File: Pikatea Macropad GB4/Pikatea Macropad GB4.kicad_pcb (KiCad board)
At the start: 2 copper layers, 125.1 x 25.2 mm, 28 parts, among them J1 AVR-ISP-6, J2 USB_B_Mini, J4 Conn_01x03_Male, J5 Conn_01x03_Male, J6 Conn_01x06_Male, SW1 SW_DPST, SW2 Rotary_Encoder_Switch, U1 ATMEGA32U4-EP, X1 16MHz

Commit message: update GB4
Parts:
- removed J5: Conn_01x03_Male, Connector_PinHeader_2.54mm:PinHeader_1x03_P2.54mm_Vertical
- added D2: APA-106-F5, Pikatea:TONYU-DY-S352818-RGBC, B.Cu at (149.9, 109.7)
- added D3: APA-106-F5, Pikatea:TONYU-DY-S352818-RGBC, B.Cu at (168.9, 109.7)
- added D4: APA-106-F5, Pikatea:TONYU-DY-S352818-RGBC, B.Cu at (188.0, 109.7)
- added D5: APA-106-F5, Pikatea:TONYU-DY-S352818-RGBC, B.Cu at (207.1, 109.7)
- added D6: APA-106-F5, Pikatea:TONYU-DY-S352818-RGBC, F.Cu at (220.7, 110.0)
- added D7: APA-106-F5, Pikatea:TONYU-DY-S352818-RGBC, F.Cu at (230.6, 110.3)
- D1: moved to B.Cu
- U1: footprint Package_QFP:LQFP-44_10x10mm_P0.8mm -> Package_DFN_QFN:QFN-44-1EP_7x7mm_P0.5mm_EP5.15x5.15mm_ThermalVias
- moved D1 21.3 mm to (130.8, 109.7)
- moved C3 5.36 mm to (110.9, 99.7)
- moved C6 3.73 mm to (130.9, 96.3)
- moved C4 1.35 mm to (125.6, 99.8), turned to 90 degrees
- moved R5 0.88 mm to (129.9, 93.8)
- moved C10 0.63 mm to (124.8, 102.0)
- turned MX1 to 180 degrees
- turned MX2 to 180 degrees
- turned MX3 to 180 degrees
- turned MX4 to 180 degrees
- turned MX5 to 180 degrees
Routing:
- net VBUS: track 0.00 -> 103.3 mm, vias 0 -> 7
- net /A0: track 0.00 -> 86.9 mm
- net GND: track 0.00 -> 41.5 mm, vias 0 -> 3
- net Net-(D1-Pad1): track 0.00 -> 14.6 mm
- net Net-(D4-Pad1): track 0.00 -> 14.6 mm
- net Net-(D2-Pad1): track 0.00 -> 14.6 mm
- net /D3: track 0.00 -> 13.3 mm
- net Net-(C8-Pad1): track 0.00 -> 12.6 mm
- net Net-(C7-Pad1): track 0.00 -> 11.3 mm
- net Net-(R5-Pad2): track 0.00 -> 9.35 mm
- net Net-(R4-Pad2): track 0.00 -> 9.26 mm
- net Net-(C9-Pad1): track 0.00 -> 8.24 mm
- net /D4: track 0.00 -> 7.75 mm
- net /D+: track 0.00 -> 6.50 mm
- net /D-: track 0.00 -> 5.83 mm
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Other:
- outline, holes or cut-outs redrawn

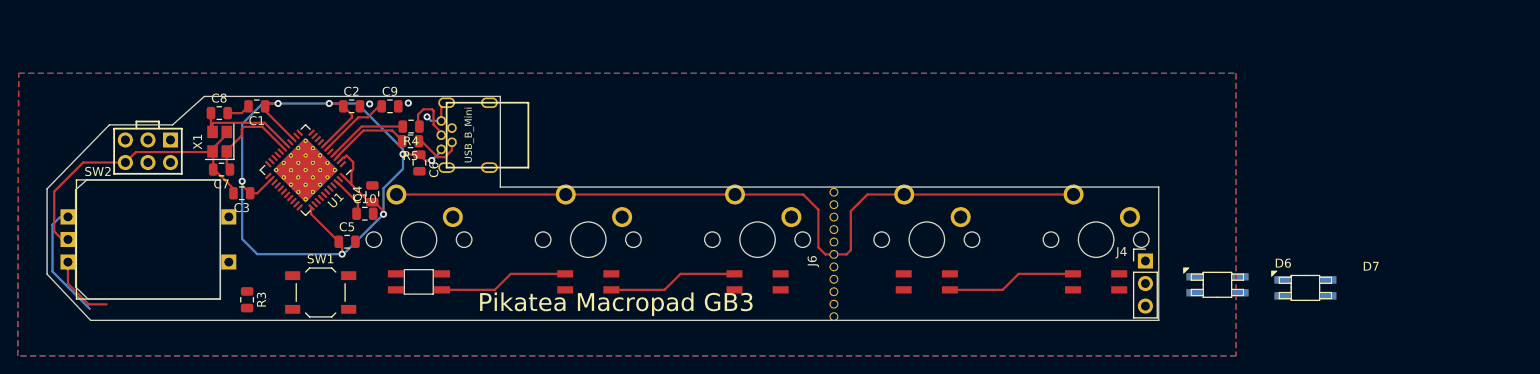
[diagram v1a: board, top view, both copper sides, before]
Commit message: update r26 and gb4
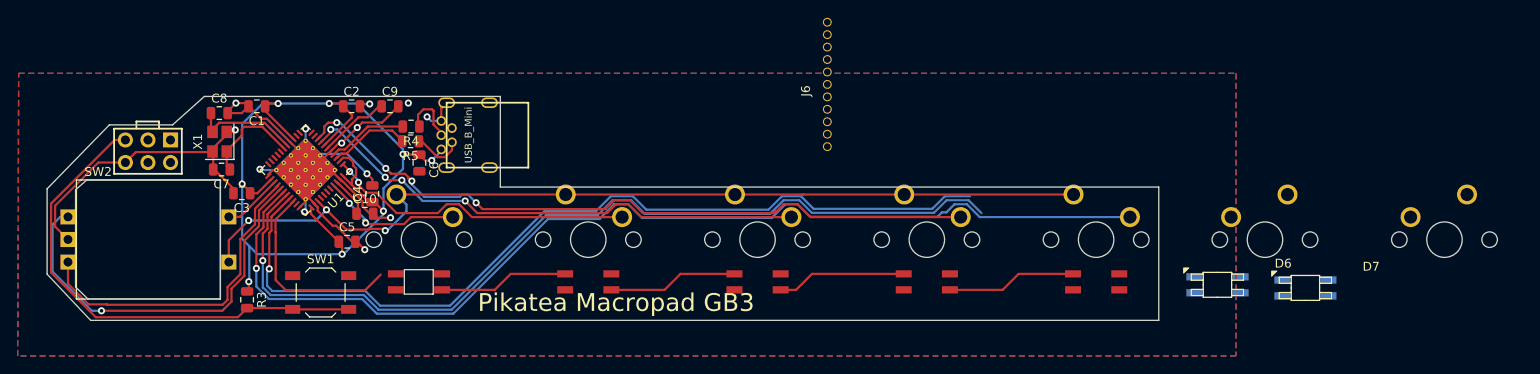
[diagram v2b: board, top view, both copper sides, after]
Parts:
- removed J4: Conn_01x03_Male, Connector_PinHeader_2.54mm:PinHeader_1x03_P2.54mm_Vertical
- added MX6: MX-LED, MX_Only:MXOnly-1U-NoLED, F.Cu at (226.1, 104.9)
- added MX7: MX-LED, MX_Only:MXOnly-1U-NoLED, F.Cu at (246.2, 104.9)
- moved J6 19.1 mm to (176.8, 87.5)
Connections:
- D1 pad 4: Net-(D1-Pad4) -> /31
- J1 pad 3: /SCK -> /D8
- J6 pad 1: GND -> Net-(J6-Pad1)
- J6 pad 2: /D8 -> Net-(J6-Pad2)
- J6 pad 3: /D6 -> Net-(J6-Pad3)
- J6 pad 4: /A0 -> Net-(J6-Pad4)
- J6 pad 5: /D1 -> Net-(J6-Pad5)
- J6 pad 6: /D0 -> Net-(J6-Pad6)
- MX5 pad 1: /D6 -> /28
- SW2 pad A: /D4 -> /D12
- SW2 pad B: /D3 -> /D6
- SW2 pad S1: /D2 -> /D4
- U1 pad 1: /D7 -> /D9
- U1 pad 28: /D8 -> /28
- U1 pad 29: /D9 -> /29
- U1 pad 31: /D5 -> /31
- U1 pad 41: /D0 -> /D5
- U1 pad 8: Net-(U1-Pad8) -> /D7
- U1 pad 9: /SCK -> /D8
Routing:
- net /28: track 0.00 -> 119.7 mm, vias 0 -> 1
- net /29: track 0.00 -> 101.6 mm, vias 0 -> 1
- net /CS: track 0.00 -> 98.6 mm, vias 0 -> 1
- net GND: track 41.5 -> 128.1 mm, vias 3 -> 13
- net /D8: track 0.00 -> 80.6 mm, vias 0 -> 4
- net /D7: track 0.00 -> 58.6 mm, vias 0 -> 4
- net /RESET: track 0.00 -> 55.1 mm
- net /D6: track 0.00 -> 44.8 mm, vias 0 -> 1
- net /D12: track 0.00 -> 36.8 mm
- net /D9: track 0.00 -> 35.1 mm, vias 0 -> 2
- net /31: track 0.00 -> 22.8 mm
- net /A0: track 86.9 -> 105.7 mm, vias 0 -> 3
- net /D5: track 0.00 -> 15.9 mm, vias 0 -> 2
- net Net-(D3-Pad1): track 0.00 -> 14.6 mm
- net /D3: track 13.3 -> 0.00 mm
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
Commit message: Revision b of GB4
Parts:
- removed J6: Conn_01x06_Male, Pikatea Macropad Encoder Side Mount:Breakaway-Throughole
- added J3: Conn_01x11_Female, Pikatea:Breakaway-Throughole-GB4, F.Cu at (176.6, 106.2)
- added J4: Conn_01x11_Female, Pikatea:Breakaway-Throughole-GB4, F.Cu at (214.6, 106.2)
- D6, D7, MX6, MX7: moved to B.Cu
- moved D7 14.6 mm to (245.2, 109.7)
- moved D6 5.41 mm to (226.1, 109.7)
- moved MX7 1.10 mm to (245.2, 104.9), turned to 180 degrees
- moved C8 0.29 mm to (108.1, 90.6)
- turned MX6 to 180 degrees
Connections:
- D1 pad 2: Net-(D1-Pad2) -> GND
- D1 pad 3: Net-(D1-Pad3) -> VBUS
- D2 pad 2: Net-(D2-Pad2) -> GND
- D2 pad 3: Net-(D2-Pad3) -> VBUS
- D3 pad 2: Net-(D3-Pad2) -> GND
- D3 pad 3: Net-(D3-Pad3) -> VBUS
- D4 pad 2: Net-(D4-Pad2) -> GND
- D4 pad 3: Net-(D4-Pad3) -> VBUS
- D5 pad 2: Net-(D5-Pad2) -> GND
- D5 pad 3: Net-(D5-Pad3) -> VBUS
- D6 pad 2: Net-(D6-Pad2) -> GND
- D6 pad 3: Net-(D6-Pad3) -> VBUS
- D7 pad 2: Net-(D7-Pad2) -> GND
- D7 pad 3: Net-(D7-Pad3) -> VBUS
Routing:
- net VBUS: track 108.0 -> 251.9 mm
- net GND: track 128.1 -> 220.0 mm, vias 13 -> 57
- net /CS: track 98.6 -> 158.1 mm
- net /29: track 101.6 -> 140.6 mm
- net /A0: track 105.7 -> 144.2 mm
- net /D8: track 80.6 -> 114.0 mm, vias 4 -> 9
- net /MOSI: track 0.00 -> 24.9 mm, vias 0 -> 3
- net /RESET: track 55.1 -> 78.0 mm, vias 0 -> 4
- net /MISO: track 0.00 -> 21.5 mm, vias 0 -> 2
- net Net-(D6-Pad1): track 0.00 -> 14.6 mm
- net Net-(D5-Pad1): track 0.00 -> 14.6 mm
- net /D9: track 35.1 -> 41.2 mm
- net Net-(C8-Pad1): track 12.2 -> 7.13 mm
- net /28: track 119.7 -> 122.6 mm
- net /31: track 22.8 -> 24.5 mm
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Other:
- board size 125.1 x 25.2 mm -> 163.2 x 25.2 mm
- board text added: "!print"
- board text added: "Pikatea Macropad GB4"
- board text removed: "Pikatea Macropad GB3"

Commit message: update gb4 to kicad 6, add gb4 fkvarient
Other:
- net class Default removed
